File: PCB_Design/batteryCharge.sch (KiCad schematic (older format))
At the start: 9 parts

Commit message: arreglo estetico de esquematico
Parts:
- gave numbers to parts that had none: 9
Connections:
- wire segments 24 -> 29
- no-connect marks 1 -> 0
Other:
- moved on the sheet: C1, C2, J, R_5v, R_PROG, R_gLED, R_rLED, gLED, rLED

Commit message: Partialy finished schematic
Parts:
- added Battery: Battery_Cell, symbol Device:Battery_Cell
- added USB_carga: USB_C_Plug_USB2.0, symbol Connector:USB_C_Plug_USB2.0
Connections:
- net labels removed: +5V
- wire segments 29 -> 37
- no-connect marks 0 -> 4
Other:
- moved on the sheet: C1, C2, J, R_5v, R_PROG, R_gLED, R_rLED, gLED, rLED

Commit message: huellas agregadas
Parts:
- removed R_5v: 0.4, symbol Device:R
- removed USB_carga: USB_C_Plug_USB2.0, symbol Connector:USB_C_Plug_USB2.0
- added Battery2: Battery_Cell, Battery:BatteryHolder_MPD_BH-18650-PC2, symbol Device:Battery_Cell
- added J2: 632723300011, Connector_USB:632723300011, symbol 632723300011:632723300011
- Battery1: renamed from Battery; footprint (none) -> Battery:BatteryHolder_MPD_BH-18650-PC2
- C1, C2: footprint (none) -> Capacitor_SMD:CP_Elec_4x5.8
- J1: renamed from J; footprint SOIC127P600X175-9N -> Package_SO:SOIC-8-1EP_3.9x4.9mm_P1.27mm_EP2.514x3.2mm
- R_PROG1: renamed from R_PROG; footprint (none) -> Resistor_SMD:R_0805_2012Metric_Pad1.20x1.40mm_HandSolder
- R_gLED1: renamed from R_gLED; footprint (none) -> Resistor_SMD:R_0805_2012Metric_Pad1.20x1.40mm_HandSolder
- R_rLED1: renamed from R_rLED; footprint (none) -> Resistor_SMD:R_0805_2012Metric_Pad1.20x1.40mm_HandSolder
- gLED1: renamed from gLED; footprint (none) -> LED_SMD:LED_0805_2012Metric_Pad1.15x1.40mm_HandSolder
- rLED1: renamed from rLED; footprint (none) -> LED_SMD:LED_0805_2012Metric_Pad1.15x1.40mm_HandSolder
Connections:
- wire segments 37 -> 59
- no-connect marks 4 -> 22
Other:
- moved on the sheet: Battery1, C1, C2, J1, R_PROG1, R_gLED1, R_rLED1, gLED1, rLED1

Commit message: Falta tetris
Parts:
- J2: symbol 632723300011:632723300011 -> PCB_Design-rescue:632723300011-632723300011
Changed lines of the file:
@@
 Connection ~ 3945 4160
 $Comp
-L 632723300011:632723300011 J2
+L PCB_Design-rescue:632723300011-632723300011 J2
 U 1 1 61D27D8A
 P 4830 770
+AR Path="/61D27D8A" Ref="J2"  Part="1"
+AR Path="/619FECCC/61D27D8A" Ref="J2"  Part="1"
 F 0 "J2" V 5375 105 50  0000 L CNN
 F 1 "632723300011" V 5485 -230 50  0000 L CNN

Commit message: Nuevas huellas y un poco más de orden
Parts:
- C1, C2: footprint Capacitor_SMD:CP_Elec_4x5.8 -> Capacitor_SMD:C_0805_2012Metric_Pad1.18x1.45mm_HandSolder
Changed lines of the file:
@@
 F 0 "C1" H 950 3251 50  0000 L CNN
 F 1 "10u" H 950 3160 50  0000 L CNN
-F 2 "Capacitor_SMD:CP_Elec_4x5.8" H 873 3055 50  0001 C CNN
+F 2 "Capacitor_SMD:C_0805_2012Metric_Pad1.18x1.45mm_HandSolder" H 873 3055 50  0001 C CNN
 F 3 "~" H 835 3205 50  0001 C CNN
 	1    835  3205
@@
 F 0 "C2" H 3610 3231 50  0000 L CNN
 F 1 "10u" H 3610 3140 50  0000 L CNN
-F 2 "Capacitor_SMD:CP_Elec_4x5.8" H 3533 3035 50  0001 C CNN
+F 2 "Capacitor_SMD:C_0805_2012Metric_Pad1.18x1.45mm_HandSolder" H 3533 3035 50  0001 C CNN
 F 3 "~" H 3495 3185 50  0001 C CNN
 	1    3495 3185

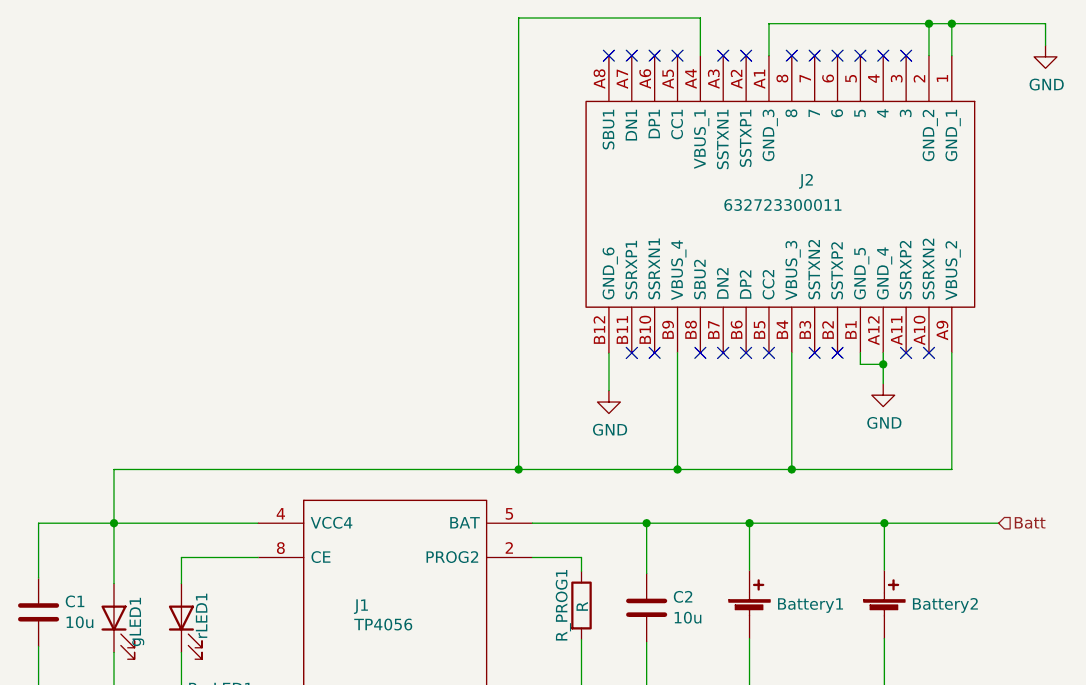
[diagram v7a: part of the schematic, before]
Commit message: PCB final con usb B micro, y modelo 3D de la placa
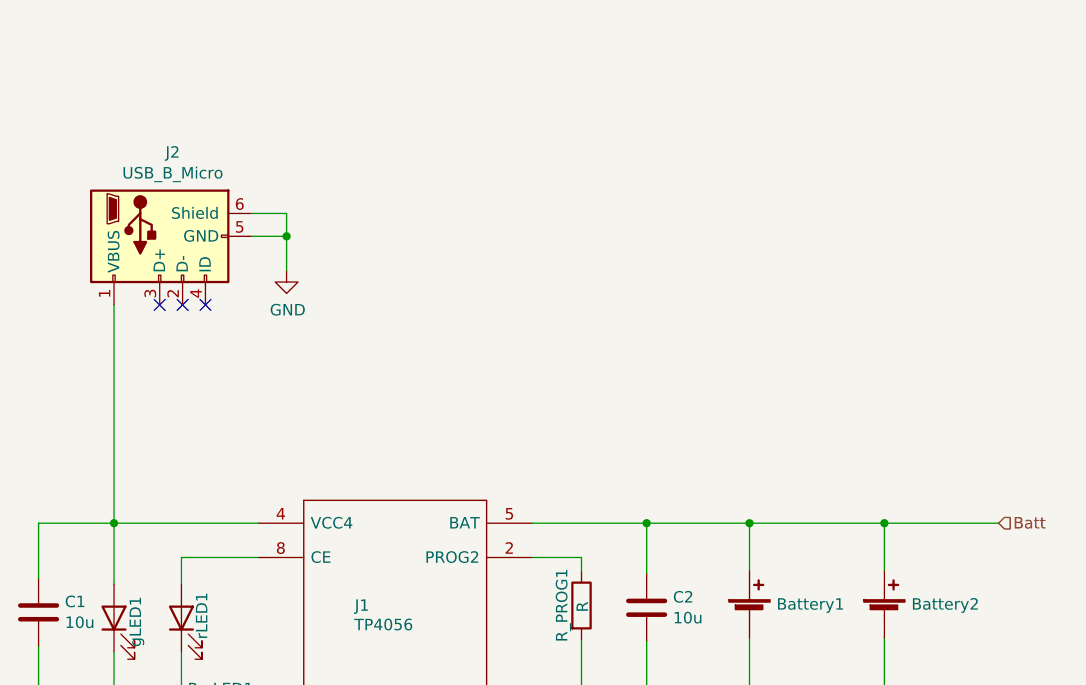
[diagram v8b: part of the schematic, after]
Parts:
- removed J2: 632723300011, Connector_USB:632723300011, symbol PCB_Design-rescue:632723300011-632723300011
- added J2: USB_B_Micro, Connector_USB:USB_Micro-B_Molex_47346-0001, symbol Connector:USB_B_Micro
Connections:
- wire segments 59 -> 41
- no-connect marks 22 -> 3
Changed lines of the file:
@@
 Connection ~ 3945 4160
 $Comp
-L PCB_Design-rescue:632723300011-632723300011 J2
-U 1 1 61D27D8A
-P 4830 770
-AR Path="/61D27D8A" Ref="J2"  Part="1"
-AR Path="/619FECCC/61D27D8A" Ref="J2"  Part="1"
-F 0 "J2" V 5375 105 50  0000 L CNN
-F 1 "632723300011" V 5485 -230 50  0000 L CNN
-F 2 "Connector_USB:632723300011" H 5980 870 50  0001 L CNN
-F 3 "http://katalog.we-online.de/em/datasheet/632723x00011.pdf" H 5980 770 50  0001 L CNN
-F 4 "USB Connectors WR-COM USB3.1 Type C SuperSpeed+ Rcpt" H 5980 670 50  0001 L CNN "Description"
-F 5 "2" H 5980 570 50  0001 L CNN "Height"
-F 6 "Wurth Elektronik" H 5980 470 50  0001 L CNN "Manufacturer_Name"
-F 7 "632723300011" H 5980 370 50  0001 L CNN "Manufacturer_Part_Number"
-F 8 "710-632723300011" H 5980 270 50  0001 L CNN "Mouser Part Number"
-F 9 "https://www.mouser.co.uk/ProductDetail/Wurth-Elektronik/632723300011?qs=NK6InXoXhq4%252B5eM1PePLPg%3D%3D" H 5980 170 50  0001 L CNN "Mouser Price/Stock"
-F 10 "" H 5980 70  50  0001 L CNN "Arrow Part Number"
-F 11 "" H 5980 -30 50  0001 L CNN "Arrow Price/Stock"
-	1    4830 770
-	0    1    1    0
+L Connector:USB_B_Micro J2
+U 1 1 61D5126A
+P 1365 1560
+F 0 "J2" V 998 1503 50  0000 C CNN
+F 1 "USB_B_Micro" V 1089 1503 50  0000 C CNN
+F 2 "Connector_USB:USB_Micro-B_Molex_47346-0001" H 1515 1510 50  0001 C CNN
+F 3 "~" H 1515 1510 50  0001 C CNN
+	1    1365 1560
+	0    -1   1    0
 $EndComp
-NoConn ~ 4730 2070
-NoConn ~ 4630 2070
-NoConn ~ 4330 2070
-NoConn ~ 4230 2070
-NoConn ~ 4030 2070
-NoConn ~ 3930 2070
-NoConn ~ 3830 2070
-NoConn ~ 3730 2070
-NoConn ~ 3530 2070
-NoConn ~ 3430 2070
-NoConn ~ 3330 770
-NoConn ~ 3430 770
-NoConn ~ 3530 770
-NoConn ~ 3630 770
-NoConn ~ 3830 770
-NoConn ~ 3930 770
-NoConn ~ 4130 770
-NoConn ~ 4230 770
-NoConn ~ 4330 770
-NoConn ~ 4430 770
-NoConn ~ 4530 770
-NoConn ~ 4630 770
+Wire Wire Line
+	1165 1860 1165 2815
+NoConn ~ 1365 1860
+NoConn ~ 1465 1860
+NoConn ~ 1565 1860
 $Comp
 L power:GND #PWR0123
-U 1 1 61D348B7
-P 3330 2235
-F 0 "#PWR0123" H 3330 1985 50  0001 C CNN
-F 1 "GND" H 3335 2062 50  0000 C CNN
-F 2 "" H 3330 2235 50  0001 C CNN
-F 3 "" H 3330 2235 50  0001 C CNN
-	1    3330 2235
-	1    0    0    -1
-$EndComp
-$Comp
-L power:GND #PWR0124
-U 1 1 61D35F5F
-P 4530 2205
-F 0 "#PWR0124" H 4530 1955 50  0001 C CNN
-F 1 "GND" H 4535 2032 50  0000 C CNN
-F 2 "" H 4530 2205 50  0001 C CNN
-F 3 "" H 4530 2205 50  0001 C CNN
-	1    4530 2205
-	1    0    0    -1
-$EndComp
-$Comp
-L power:GND #PWR0125
-U 1 1 61D3637C
-P 5240 725
-F 0 "#PWR0125" H 5240 475 50  0001 C CNN
-F 1 "GND" H 5245 552 50  0000 C CNN
-F 2 "" H 5240 725 50  0001 C CNN
-F 3 "" H 5240 725 50  0001 C CNN
-	1    5240 725
+U 1 1 61D5A238
+P 1920 1710
+F 0 "#PWR0123" H 1920 1460 50  0001 C CNN
+F 1 "GND" H 1925 1537 50  0000 C CNN
+F 2 "" H 1920 1710 50  0001 C CNN
+F 3 "" H 1920 1710 50  0001 C CNN
+	1    1920 1710
 	1    0    0    -1
 $EndComp
 Wire Wire Line
-	4530 2070 4530 2120
+	1920 1460 1765 1460
 Wire Wire Line
-	4430 2120 4430 2070
+	1765 1560 1920 1560
 Wire Wire Line
-	4430 2120 4530 2120
-Connection ~ 4530 2120
+	1920 1460 1920 1560
+Connection ~ 1920 1560
 Wire Wire Line
-	4530 2120 4530 2205
-Wire Wire Line
-	3330 2070 3330 2235
-Wire Wire Line
-	4730 770  4730 630
-Wire Wire Line
-	4730 630  4830 630
-Wire Wire Line
-	5240 630  5240 725
-Wire Wire Line
-	4830 770  4830 630
-Connection ~ 4830 630
-Wire Wire Line
-	4830 630  5240 630
-Wire Wire Line
-	4830 2070 4830 2580
-Wire Wire Line
-	4830 2580 4130 2580
-Wire Wire Line
-	1165 2580 1165 2815
-Wire Wire Line
-	4130 2070 4130 2580
-Connection ~ 4130 2580
-Wire Wire Line
-	4130 2580 3630 2580
-Wire Wire Line
-	3630 2070 3630 2580
-Connection ~ 3630 2580
-Wire Wire Line
-	3630 2580 2935 2580
-Wire Wire Line
-	2935 605  2935 2580
-Wire Wire Line
-	3730 770  3730 605
-Wire Wire Line
-	3730 605  2935 605
-Wire Wire Line
-	4030 770  4030 630
-Wire Wire Line
-	4030 630  4730 630
-Connection ~ 4730 630
-Connection ~ 2935 2580
-Wire Wire Line
-	2935 2580 1165 2580
+	1920 1560 1920 1710
 $EndSCHEMATC
